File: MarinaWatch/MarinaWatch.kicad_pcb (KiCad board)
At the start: 2 copper layers, 2 parts, among them J1 USB_C_Receptacle_USB2.0_16P, U1 ESP32-S3-WROOM-1

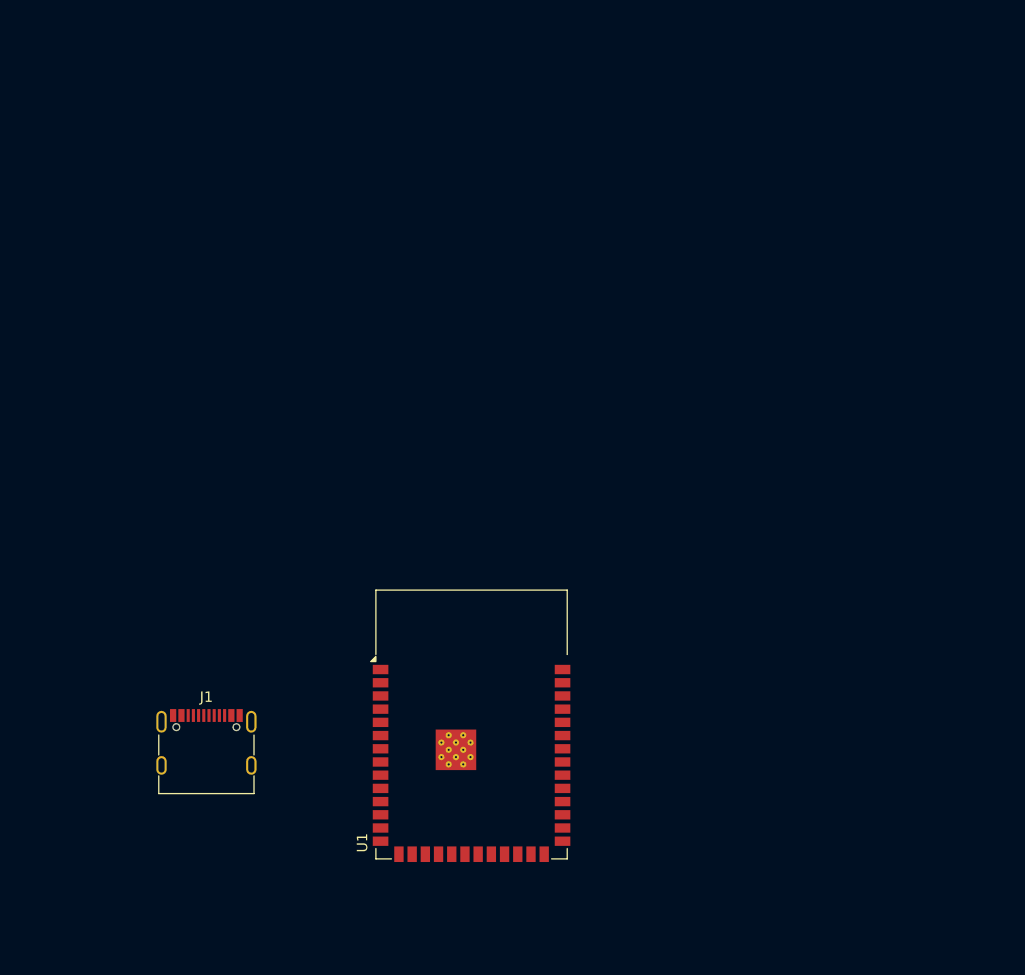
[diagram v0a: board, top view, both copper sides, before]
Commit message: Finished USB hardware. Started power supply.
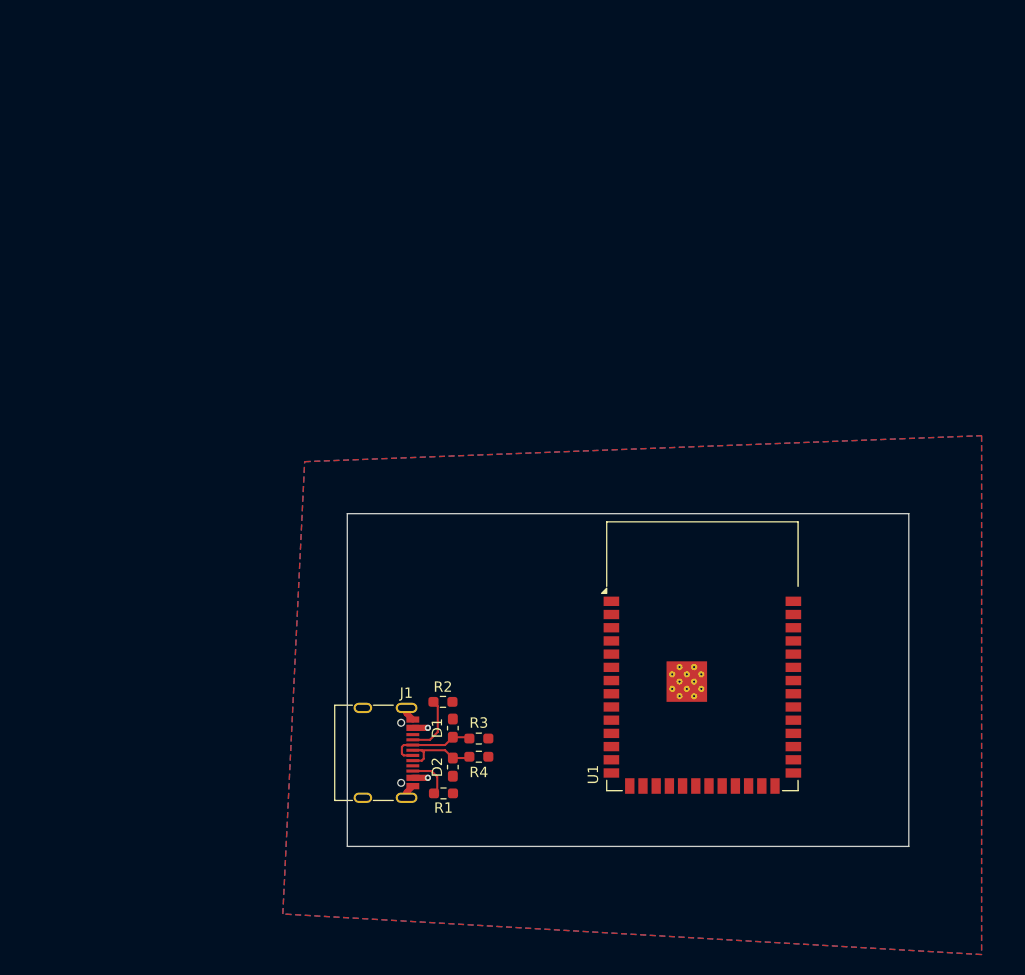
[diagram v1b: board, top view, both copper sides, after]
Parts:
- added D1: D_TVS, Fuse:Fuse_0603_1608Metric_Pad1.05x0.95mm_HandSolder, F.Cu at (110.2, 88.6)
- added D2: D_TVS, Fuse:Fuse_0603_1608Metric_Pad1.05x0.95mm_HandSolder, F.Cu at (110.2, 92.4)
- added R1: 5k1, Resistor_SMD:R_0603_1608Metric_Pad0.98x0.95mm_HandSolder, F.Cu at (109.2, 94.9)
- added R2: 5k1, Resistor_SMD:R_0603_1608Metric_Pad0.98x0.95mm_HandSolder, F.Cu at (109.2, 86.1)
- added R3: 22R, Resistor_SMD:R_0603_1608Metric_Pad0.98x0.95mm_HandSolder, F.Cu at (112.7, 89.6)
- added R4: 22R, Resistor_SMD:R_0603_1608Metric_Pad0.98x0.95mm_HandSolder, F.Cu at (112.7, 91.4)
- moved U1 23.1 mm to (134.2, 81.7)
- moved J1 16.1 mm to (102.6, 91.0), turned to -90 degrees
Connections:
- net Net-(J1-VBUS-PadA4) renamed VBUS
- J1 pad A5: unconnected-(J1-CC1-PadA5) -> /CC1
- J1 pad A6: unconnected-(J1-D+-PadA6) -> /USB_D+
- J1 pad A7: unconnected-(J1-D--PadA7) -> /USB_D-
- J1 pad B5: unconnected-(J1-CC2-PadB5) -> /CC2
- J1 pad B6: unconnected-(J1-D+-PadB6) -> /USB_D+
- J1 pad B7: unconnected-(J1-D--PadB7) -> /USB_D-
- J1 pad S1: unconnected-(J1-SHIELD-PadS1) -> GND
- U1 pad 13: unconnected-(U1-IO19-Pad13) -> /ESP_D-
- U1 pad 14: unconnected-(U1-IO20-Pad14) -> /ESP_D+
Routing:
- net /USB_D-: track 0.00 -> 8.69 mm
- net /USB_D+: track 0.00 -> 7.94 mm
- net /CC1: track 0.00 -> 5.78 mm
- net /CC2: track 0.00 -> 4.31 mm
- net VBUS: track 0.00 -> 2.90 mm, vias 0 -> 2
- net GND: track 0.00 -> 2.74 mm
- added copper zone on B.Cu, net GND
- added copper zone on F.Cu, net GND
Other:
- board outline added: 54 x 32 mm

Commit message: Structure power supply chain
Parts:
- added C1: 1u, Capacitor_SMD:C_0603_1608Metric_Pad1.08x0.95mm_HandSolder, F.Cu at (104.4, 78.2)
- added C10: 10u, Capacitor_SMD:C_0603_1608Metric_Pad1.08x0.95mm_HandSolder, F.Cu at (112.2, 60.8)
- added C11: 10u, Capacitor_SMD:C_0603_1608Metric_Pad1.08x0.95mm_HandSolder, F.Cu at (112.2, 52.5)
- added C12: 10u, Capacitor_SMD:C_0603_1608Metric_Pad1.08x0.95mm_HandSolder, F.Cu at (112.2, 54.4)
- added C2: 1u, Capacitor_SMD:C_0603_1608Metric_Pad1.08x0.95mm_HandSolder, F.Cu at (106.0, 78.2)
- added C3: 1u, Capacitor_SMD:C_0603_1608Metric_Pad1.08x0.95mm_HandSolder, F.Cu at (104.4, 73.0)
- added C5: 1u, Capacitor_SMD:C_0603_1608Metric_Pad1.08x0.95mm_HandSolder, F.Cu at (114.1, 81.0)
- added C6: 1u, Capacitor_SMD:C_0603_1608Metric_Pad1.08x0.95mm_HandSolder, F.Cu at (106.0, 67.2)
- added C7: 1u, Capacitor_SMD:C_0603_1608Metric_Pad1.08x0.95mm_HandSolder, F.Cu at (112.1, 63.3)
- added C8: 4u7, Capacitor_SMD:C_0603_1608Metric_Pad1.08x0.95mm_HandSolder, F.Cu at (106.0, 73.0)
- added C9: 100n, Capacitor_SMD:C_0603_1608Metric_Pad1.08x0.95mm_HandSolder, F.Cu at (116.0, 57.9)
- added IC1: 2609011181000, Lund Formula Student:2609011181000, F.Cu at (136.0, 50.2)
- added J2: Screw_Terminal_01x02, TerminalBlock_Phoenix:TerminalBlock_Phoenix_MKDS-3-2-5.08_1x02_P5.08mm_Horizontal, F.Cu at (106.0, 47.7)
- added L1: 2u2, Inductor_SMD_Wurth:L_Wurth_WE-LQSH-4020, F.Cu at (109.7, 66.6)
- added L2: 2u2, Inductor_SMD_Wurth:L_Wurth_WE-LQSH-4020, F.Cu at (107.3, 57.5)
- added R10: 1k, Resistor_SMD:R_0603_1608Metric_Pad0.98x0.95mm_HandSolder, F.Cu at (111.2, 80.9)
- added R11: 100R, Resistor_SMD:R_0603_1608Metric_Pad0.98x0.95mm_HandSolder, F.Cu at (116.0, 59.8)
- added R12: 10k, Resistor_SMD:R_0603_1608Metric_Pad0.98x0.95mm_HandSolder, F.Cu at (105.2, 85.9)
- added R13: 27k, Resistor_SMD:R_0603_1608Metric_Pad0.98x0.95mm_HandSolder, F.Cu at (105.2, 84.3)
- added R5: 10k, Resistor_SMD:R_0603_1608Metric_Pad0.98x0.95mm_HandSolder, F.Cu at (111.0, 85.2)
- added R6: 10k, Resistor_SMD:R_0603_1608Metric_Pad0.98x0.95mm_HandSolder, F.Cu at (107.8, 85.2)
- added R7: 10k, Resistor_SMD:R_0603_1608Metric_Pad0.98x0.95mm_HandSolder, F.Cu at (109.5, 85.2)
- added R8: 10k, Resistor_SMD:R_0603_1608Metric_Pad0.98x0.95mm_HandSolder, F.Cu at (109.7, 71.0)
- added R9: 10k, Resistor_SMD:R_0603_1608Metric_Pad0.98x0.95mm_HandSolder, F.Cu at (105.2, 82.6)
- added TP1: TestPoint, TestPoint:TestPoint_Pad_D2.0mm, F.Cu at (102.0, 77.5)
- added TP2: TestPoint, TestPoint:TestPoint_Pad_D2.0mm, F.Cu at (102.0, 73.8)
- added TP3: TestPoint, TestPoint:TestPoint_Pad_D2.0mm, F.Cu at (80.2, 74.7)
- added TP4: TestPoint, TestPoint:TestPoint_Pad_D2.0mm, F.Cu at (112.5, 71.0)
- added TP5: TestPoint, TestPoint:TestPoint_Pad_D2.0mm, F.Cu at (115.8, 53.5)
- added U2: TPS63001, Package_SON:Texas_DRC0010J_ThermalVias, F.Cu at (112.2, 57.5)
- added U3: BQ24166RGE, Package_DFN_QFN:Texas_RGE0024H_VQFN-24-1EP_4x4mm_P0.5mm_EP2.7x2.7mm, F.Cu at (109.7, 75.6)
- moved U1 6.29 mm to (137.1, 87.2), turned to -90 degrees
- moved D1 3.68 mm to (110.2, 92.3)
- moved D2 3.68 mm to (110.2, 96.1)
- moved J1 3.68 mm to (102.6, 94.7)
- moved R2 3.68 mm to (109.2, 89.8)
- moved R3 3.68 mm to (112.7, 93.3)
- moved R4 3.68 mm to (112.7, 95.1)
- moved R1 3.68 mm to (109.2, 98.6)
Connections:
- U1 pad 2: unconnected-(U1-3V3-Pad2) -> +3.3V
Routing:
- net VDD: track 0.00 -> 39.1 mm, vias 0 -> 2
- net VBUS: track 2.90 -> 25.2 mm, vias 2 -> 3
- net /VDPM: track 0.00 -> 9.34 mm
- net /IUSB1: track 0.00 -> 7.22 mm
- net /IUSB3: track 0.00 -> 7.20 mm
- net VCC: track 0.00 -> 7.11 mm, vias 0 -> 3
- net /BOOT: track 0.00 -> 6.99 mm
- net /IUSB2: track 0.00 -> 6.76 mm
- net /CE: track 0.00 -> 6.46 mm
- net /DRV: track 0.00 -> 4.34 mm
- net +3.3V: track 0.00 -> 4.11 mm
- net /ISET: track 0.00 -> 2.79 mm
- net GND: track 2.74 -> 5.17 mm, vias 0 -> 6
- net /ILIM: track 0.00 -> 1.81 mm
- net /PMIDU: vias 0 -> 1
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- added copper zone on F.Cu, net +3.3V
- added copper zone on F.Cu, net /L1
- added copper zone on F.Cu, net /L2
- added copper zone on F.Cu, net /PMIDI
- added copper zone on F.Cu, net /PMIDU
- added copper zone on F.Cu, net /SW
- added copper zone on F.Cu, net /VINA
- added copper zone on F.Cu, net VBUS
- added copper zone on F.Cu, net VCC
- added copper zone on F.Cu, net VDD
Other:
- board size 54 x 32 mm -> 50 x 60 mm

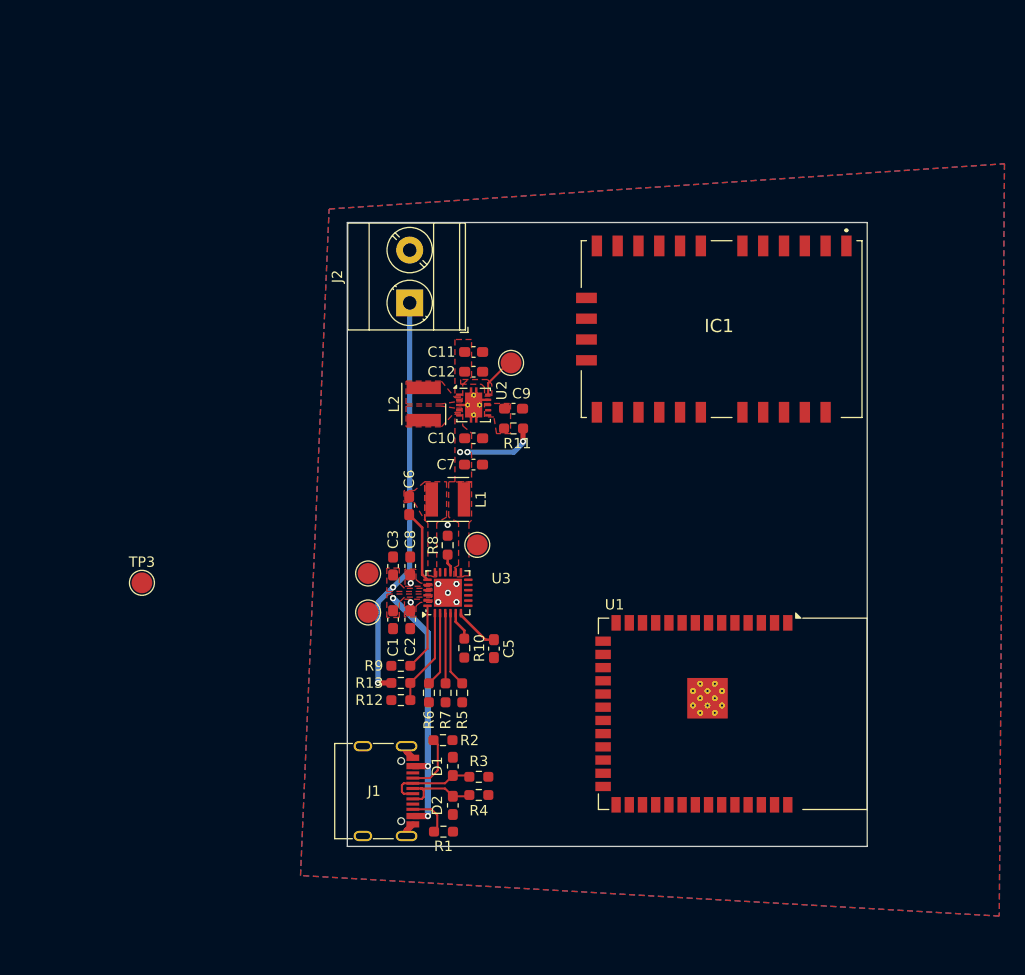
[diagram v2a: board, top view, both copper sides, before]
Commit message: Restarted HW and started testing ESP32 WiFi
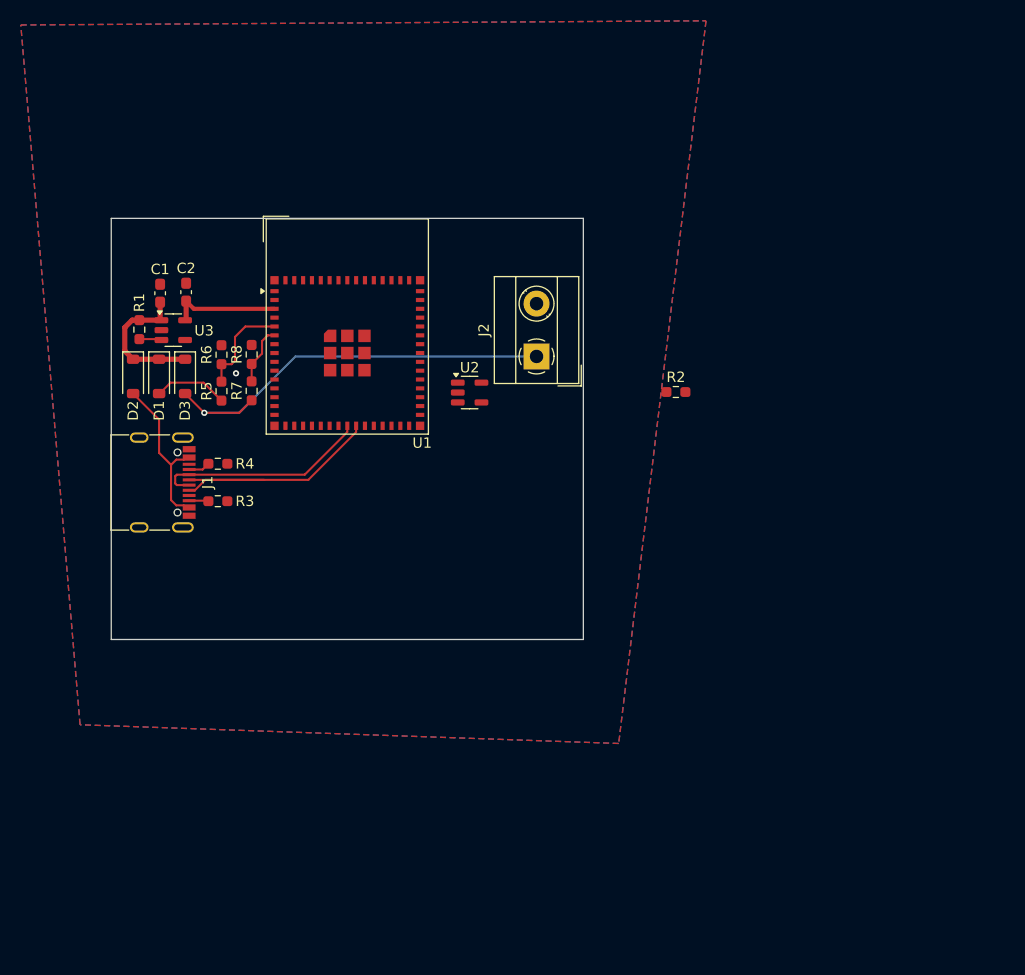
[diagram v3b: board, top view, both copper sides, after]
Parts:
- removed C10, C11, C12: 10u, Capacitor_SMD:C_0603_1608Metric_Pad1.08x0.95mm_HandSolder
- removed C3, C5, C6, C7: 1u, Capacitor_SMD:C_0603_1608Metric_Pad1.08x0.95mm_HandSolder
- removed C8: 4u7, Capacitor_SMD:C_0603_1608Metric_Pad1.08x0.95mm_HandSolder
- removed C9: 100n, Capacitor_SMD:C_0603_1608Metric_Pad1.08x0.95mm_HandSolder
- removed IC1: 2609011181000, Lund Formula Student:2609011181000
- removed L1, L2: 2u2, Inductor_SMD_Wurth:L_Wurth_WE-LQSH-4020
- removed R10: 1k, Resistor_SMD:R_0603_1608Metric_Pad0.98x0.95mm_HandSolder
- removed R11: 100R, Resistor_SMD:R_0603_1608Metric_Pad0.98x0.95mm_HandSolder
- removed R12, R9: 10k, Resistor_SMD:R_0603_1608Metric_Pad0.98x0.95mm_HandSolder
- removed R13: 27k, Resistor_SMD:R_0603_1608Metric_Pad0.98x0.95mm_HandSolder
- removed TP1, TP2, TP3, TP4, TP5: TestPoint, TestPoint:TestPoint_Pad_D2.0mm
- added D3: 1N5819, Diode_SMD:D_SOD-123, F.Cu at (84.4, 54.8)
- C1, C2: value 1u -> 10u
- D1, D2: value D_TVS -> 1N5819; footprint Fuse:Fuse_0603_1608Metric_Pad1.05x0.95mm_HandSolder -> Diode_SMD:D_SOD-123
- J2: footprint TerminalBlock_Phoenix:TerminalBlock_Phoenix_MKDS-3-2-5.08_1x02_P5.08mm_Horizontal -> TerminalBlock_MetzConnect:TerminalBlock_MetzConnect_Type101_RT01602HBWC_1x02_P5.08mm_Horizontal
- R1, R2: value 5k1 -> 12k
- R3, R4: value 22R -> 5k1
- R5, R6, R7, R8: value 10k -> 5k1
- U1: value ESP32-S3-WROOM-1 -> ESP32-S3-MINI-1; footprint RF_Module:ESP32-S3-WROOM-1 -> RF_Module:ESP32-S2-MINI-1
- U2: value TPS63001 -> MCP73831-2-OT; footprint Package_SON:Texas_DRC0010J_ThermalVias -> Package_TO_SOT_SMD:SOT-23-5
- U3: value BQ24166RGE -> AP2112K-3.3; footprint Package_DFN_QFN:Texas_RGE0024H_VQFN-24-1EP_4x4mm_P0.5mm_EP2.7x2.7mm -> Package_TO_SOT_SMD:SOT-23-5
- moved R1 56.4 mm to (80.0, 50.3), turned to -90 degrees
- moved U1 52.6 mm to (100.0, 50.0), turned to 0 degrees
- moved D2 51.5 mm to (79.4, 54.8), turned to -90 degrees
- moved D1 47.0 mm to (81.9, 54.8)
- moved R4 40.6 mm to (87.5, 63.2)
- moved R2 40.3 mm to (131.6, 56.3)
- moved C1 38.6 mm to (82.0, 46.8), turned to 90 degrees
- moved C2 38.2 mm to (84.5, 46.7), turned to 90 degrees
- moved R6 38.1 mm to (87.9, 52.7), turned to 90 degrees
- moved R5 37.1 mm to (87.9, 56.2)
- moved J1 36.7 mm to (81.1, 65.0)
- moved U3 36.5 mm to (83.3, 50.4), turned to 0 degrees
- moved R3 36.5 mm to (87.5, 66.8)
- moved R7 34.5 mm to (90.8, 56.2), turned to 90 degrees
- moved R8 26.3 mm to (90.8, 52.7)
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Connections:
- C1 pad 1: VBUS -> VCC
- C2 pad 1: /PMIDU -> +3V3
- D1 pad 1: GND -> VCC
- D1 pad 2: /USB_D- -> +BATT
- D2 pad 1: GND -> VCC
- D2 pad 2: /USB_D+ -> VBUS
- J1 pad A5: /CC1 -> Net-(J1-CC1)
- J1 pad A6: /USB_D+ -> /D+
- J1 pad A7: /USB_D- -> /D-
- J1 pad B5: /CC2 -> Net-(J1-CC2)
- J1 pad B6: /USB_D+ -> /D+
- J1 pad B7: /USB_D- -> /D-
- J2 pad 1: VDD -> SOLAR
- R1 pad 1: /CC2 -> VCC
- R1 pad 2: GND -> Net-(U3-EN)
- R2 pad 1: /CC1 -> Net-(U2-PROG)
- R3 pad 1: /USB_D- -> Net-(J1-CC2)
- R3 pad 2: /ESP_D- -> GND
- R4 pad 1: /USB_D+ -> Net-(J1-CC1)
- R4 pad 2: /ESP_D+ -> GND
- R5 pad 1: VBUS -> +BATT
- R5 pad 2: /IUSB1 -> /V_BAT
- R6 pad 1: /IUSB3 -> /V_BAT
- R7 pad 1: /IUSB2 -> SOLAR
- R7 pad 2: GND -> /V_SOLAR
- R8 pad 1: /ILIM -> /V_SOLAR
- U1 pad 13: /ESP_D- -> unconnected-(U1-IO9-Pad13)
- U1 pad 14: /ESP_D+ -> unconnected-(U1-IO10-Pad14)
- U1 pad 2: +3.3V -> GND
- U1 pad 23: unconnected-(U1-IO21-Pad23) -> /D-
- U1 pad 24: unconnected-(U1-IO47-Pad24) -> /D+
- U1 pad 3: unconnected-(U1-EN-Pad3) -> +3V3
- U1 pad 4: unconnected-(U1-IO4-Pad4) -> /BOOT
- U1 pad 40: GND -> unconnected-(U1-RXD0-Pad40)
- U1 pad 41: GND -> unconnected-(U1-IO45-Pad41)
- U1 pad 5: unconnected-(U1-IO5-Pad5) -> /V_BAT
- U1 pad 6: unconnected-(U1-IO6-Pad6) -> /V_SOLAR
- U2 pad 1: +3.3V -> unconnected-(U2-STAT-Pad1)
- U2 pad 2: /L2 -> GND
- U2 pad 3: GND -> +BATT
- U2 pad 4: /L1 -> VCC
- U2 pad 5: VCC -> Net-(U2-PROG)
- U3 pad 1: /VDPM -> VCC
- U3 pad 2: /IUSB3 -> GND
- U3 pad 3: /IUSB2 -> Net-(U3-EN)
- U3 pad 4: /IUSB1 -> unconnected-(U3-NC-Pad4)
- U3 pad 5: /ISET -> +3V3
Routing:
- net SOLAR: track 0.00 -> 41.9 mm, vias 0 -> 1
- net VDD: track 39.1 -> 0.00 mm, vias 2 -> 0
- net /D+: track 0.00 -> 26.8 mm
- net /D-: track 0.00 -> 20.7 mm
- net +3V3: track 0.00 -> 10.7 mm
- net VBUS: track 25.2 -> 15.2 mm, vias 3 -> 0
- net /V_BAT: track 0.00 -> 9.62 mm
- net /VDPM: track 9.34 -> 0.00 mm
- net /USB_D-: track 8.69 -> 0.00 mm
- net /USB_D+: track 7.94 -> 0.00 mm
- net +BATT: track 0.00 -> 7.22 mm
- net /IUSB1: track 7.22 -> 0.00 mm
- net /IUSB3: track 7.20 -> 0.00 mm
- net /BOOT: track 6.99 -> 0.00 mm
- net VCC: track 7.11 -> 14.0 mm, vias 3 -> 0
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- removed copper zone on F.Cu, net +3.3V
- removed copper zone on F.Cu, net /L1
- removed copper zone on F.Cu, net /L2
- removed copper zone on F.Cu, net /PMIDI
- removed copper zone on F.Cu, net /PMIDU
- removed copper zone on F.Cu, net /SW
- removed copper zone on F.Cu, net /VINA
- removed copper zone on F.Cu, net VBUS
- removed copper zone on F.Cu, net VCC
- removed copper zone on F.Cu, net VDD
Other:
- board size 50 x 60 mm -> 45.4 x 40.5 mm
